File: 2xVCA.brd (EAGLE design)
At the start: 100 x 39.4 mm, 50 parts, among them IC1 TL072P, IC2 LM13700N, IC3 TL072P, Q1 2N3906, Q2 2N3906, Q3 BC548B, Q4 BC548B

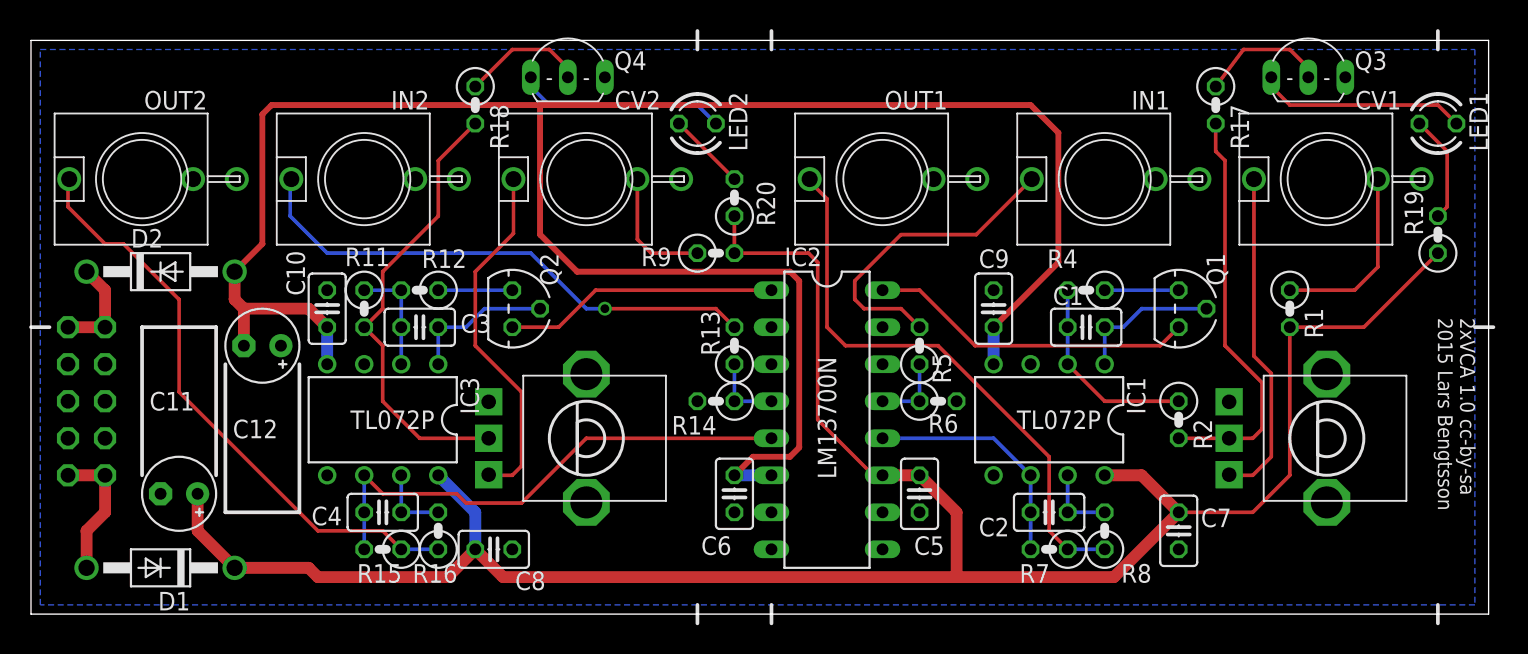
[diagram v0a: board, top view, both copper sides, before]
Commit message: Rotated CV input jacks and moved the LEDs a bit. Looks nicer this way.
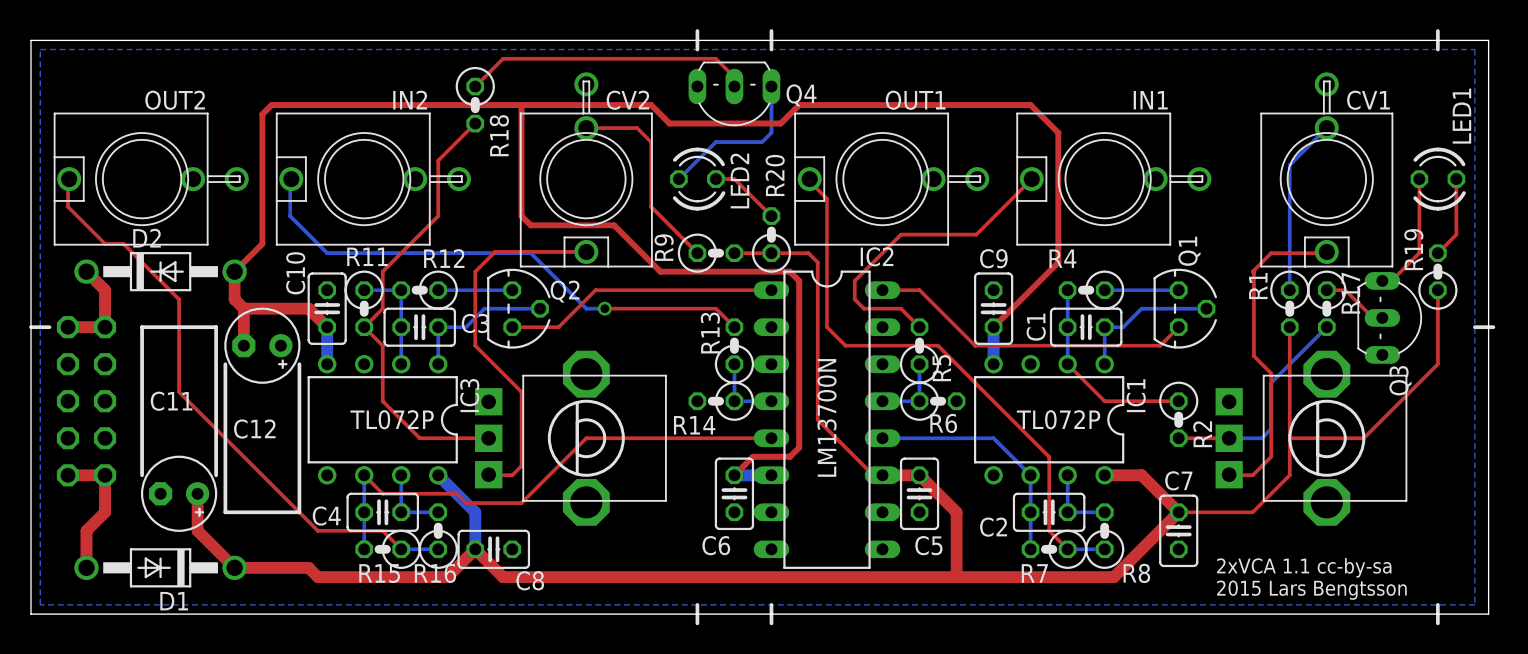
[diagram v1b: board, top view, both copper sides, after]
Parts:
- moved Q3 18.9 mm to (94.0, 21.0), turned to 270 degrees
- moved R17 15.9 mm to (88.9, 21.6)
- moved Q4 11.9 mm to (48.3, 35.6), turned to 180 degrees
- moved LED1 3.81 mm to (96.5, 30.5), turned to 180 degrees
- moved LED2 3.81 mm to (45.7, 30.5), turned to 180 degrees
- moved R20 3.59 mm to (50.8, 26.7)
- moved R19 2.54 mm to (96.5, 24.1)
- turned CV1 to 180 degrees
- turned CV2 to 180 degrees
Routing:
- net CV_ATT_1: track 28.2 -> 15.2 mm
- net N$27: track 8.56 -> 19.7 mm
- net N$24: track 14.4 -> 8.41 mm
- net N$16: track 8.65 -> 13.8 mm
- net N$4: track 8.78 -> 4.60 mm
- net N$26: track 14.4 -> 10.8 mm
- net VCC: track 153.9 -> 156.4 mm
- net N$18: track 7.40 -> 5.61 mm
- net VSS: track 146.3 -> 147.9 mm
- net N$17: track 24.6 -> 25.4 mm
- net N$3: track 23.0 -> 22.3 mm
- net N$2: track 12.7 -> 12.2 mm
- net N$25: track 5.39 -> 4.86 mm
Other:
- board text added: "2xVCA 1.1 cc-by-sa 2015 Lars Bengtsson"
- board text removed: "2xVCA 1.0 cc-by-sa 2015 Lars Bengtsson"

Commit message: Updated component values for use with 10k potentiometers.
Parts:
- R1, R9: value 33k -> 4.7k
- R10, R3: value 100k -> 10k LIN
- R11, R2: value 10k -> 33k
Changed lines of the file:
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@@
 <attribute name="VALUE" x="35.56" y="19.05" size="1.27" layer="27" ratio="10"/>
 </element>
-<element name="R1" library="rcl" package="0207/2V" value="33k" x="86.36" y="21.59" smashed="yes" rot="R270">
+<element name="R1" library="rcl" package="0207/2V" value="4.7k" x="86.36" y="21.59" smashed="yes" rot="R270">
 <attribute name="NAME" x="83.566" y="24.1808" size="1.27" layer="25" ratio="10" rot="R270"/>
 <attribute name="VALUE" x="84.1248" y="21.6408" size="1.27" layer="27" ratio="10" rot="R270"/>
 </element>
-<element name="R10" library="pot-alps" package="ALPS_POT_VERTICAL" value="100k" x="38.1" y="12.7" rot="R90"/>
-<element name="R11" library="rcl" package="0207/2V" value="10k" x="22.86" y="21.59" smashed="yes" rot="R270">
+<element name="R10" library="pot-alps" package="ALPS_POT_VERTICAL" value="10k LIN" x="38.1" y="12.7" rot="R90"/>
+<element name="R11" library="rcl" package="0207/2V" value="33k" x="22.86" y="21.59" smashed="yes" rot="R270">
 <attribute name="NAME" x="21.5392" y="24.511" size="1.27" layer="25" ratio="10"/>
 <attribute name="VALUE" x="21.5392" y="26.3398" size="1.27" layer="27" ratio="10"/>
@@
 <attribute name="VALUE" x="28.6258" y="2.2352" size="1.27" layer="27" ratio="10" rot="R180"/>
 </element>
-<element name="R2" library="rcl" package="0207/2V" value="10k" x="78.74" y="13.97" rot="R270"/>
-<element name="R3" library="pot-alps" package="ALPS_POT_VERTICAL" value="100k" x="88.9" y="12.7" rot="R90"/>
+<element name="R2" library="rcl" package="0207/2V" value="33k" x="78.74" y="13.97" rot="R270"/>
+<element name="R3" library="pot-alps" package="ALPS_POT_VERTICAL" value="10k LIN" x="88.9" y="12.7" rot="R90"/>
 <element name="R4" library="rcl" package="0207/2V" value="47k" x="72.39" y="22.86" smashed="yes" rot="R180">
 <attribute name="NAME" x="71.8058" y="25.654" size="1.27" layer="25" ratio="10" rot="R180"/>
@@
 <attribute name="VALUE" x="76.2508" y="2.8702" size="1.27" layer="27" ratio="10" rot="R180"/>
 </element>
-<element name="R9" library="rcl" package="0207/2V" value="33k" x="46.99" y="25.4" smashed="yes">
+<element name="R9" library="rcl" package="0207/2V" value="4.7k" x="46.99" y="25.4" smashed="yes">
 <attribute name="NAME" x="44.069" y="24.7142" size="1.27" layer="25" ratio="10" rot="R90"/>
 <attribute name="VALUE" x="43.7642" y="23.1648" size="1.27" layer="27" ratio="10"/>
